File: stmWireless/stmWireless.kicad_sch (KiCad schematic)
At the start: 51 parts, among them IC1 BALFLB-WL-08D3, J1 SWD, J2 CORTEX_DEBUG, J3 Conn_02x08_Top_Bottom, J4 SMA, U1 STM32WLE5CBU6, U2 AP63203WU, U3 BGS12WN6E6327, Y1 Crystal_32MHz, Y2 Crystal_32.768kHz

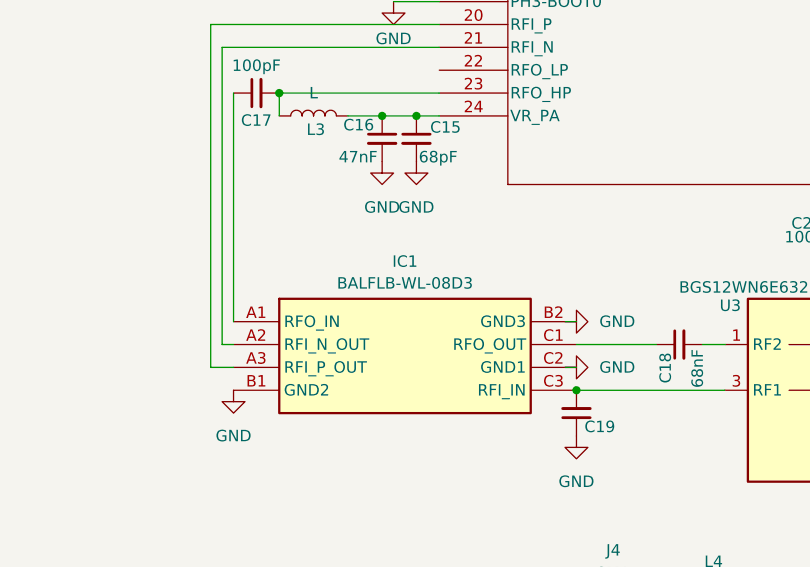
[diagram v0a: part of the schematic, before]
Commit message: substitute IPD to fix freqency
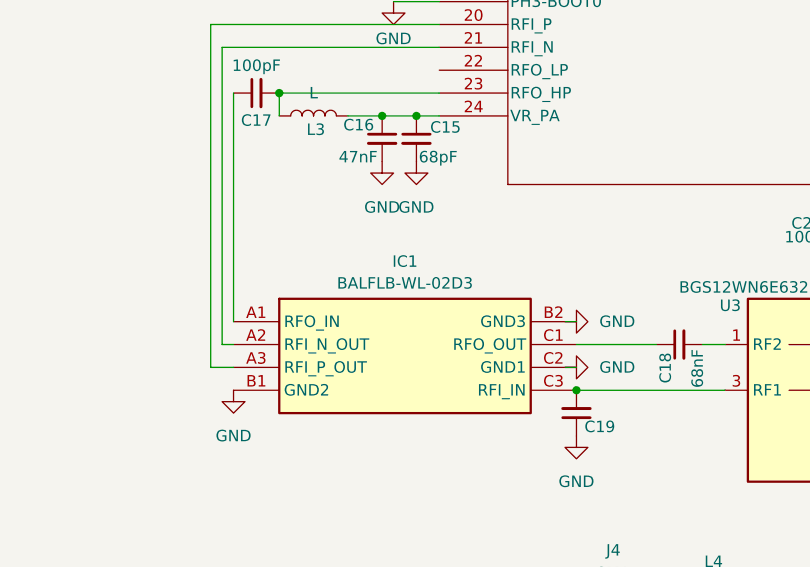
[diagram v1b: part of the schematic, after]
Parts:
- IC1: value BALFLB-WL-08D3 -> BALFLB-WL-02D3; footprint Project_library:BALFLBWL08D3 -> BALFHBWL02D3; symbol Project_library:BALFLB-WL-08D3 -> Project_library:BALFHB-WL-02D3; Manufacturer_Part_Number BALFLB-WL-08D3 -> BALFHB-WL-02D3; Mouser Part Number (none) -> 511-BALFHB-WL-02D3; Mouser Price/Stock (none) -> https://www.mouser.co.uk/ProductDetail/STMicroelectronics/B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
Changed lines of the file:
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@@
 	)
 	(symbol
-		(lib_id "Project_library:BALFLB-WL-08D3")
+		(lib_id "Project_library:BALFHB-WL-02D3")
 		(at 86.36 152.4 0)
 		(unit 1)
@@
 			)
 		)
-		(property "Value" "BALFLB-WL-08D3"
+		(property "Value" "BALFLB-WL-02D3"
 			(at 105.41 148.1398 0)
 			(effects
@@
 			)
 		)
-		(property "Footprint" "Project_library:BALFLBWL08D3"
+		(property "Footprint" "BALFHBWL02D3"
 			(at 120.65 247.32 0)
 			(effects
@@
 			)
 		)
-		(property "Datasheet" "https://www.st.com/resource/en/datasheet/balflb-wl-08d3.pdf"
+		(property "Datasheet" "https://www.st.com/resource/en/datasheet/balfhb-wl-02d3.pdf"
 			(at 120.65 347.32 0)
 			(effects
@@
 			)
 		)
-		(property "Description" "balun,filtering and matching of STM32WL 17dbm 490Mhz , QFN package 4 layers pcb"
+		(property "Description" "50  nominal input / conjugate matched balun to QFN-4L STM32WL in high power mode, 862-928 MHz with integrated harmonic filter"
 			(at 86.36 152.4 0)
 			(effects
@@
 			)
 		)
-		(property "Manufacturer_Part_Number" "BALFLB-WL-08D3"
+		(property "Manufacturer_Part_Number" "BALFHB-WL-02D3"
 			(at 120.65 747.32 0)
 			(effects
@@
 			)
 		)
-		(property "Mouser Part Number" ""
+		(property "Mouser Part Number" "511-BALFHB-WL-02D3"
 			(at 120.65 847.32 0)
 			(effects
@@
 			)
 		)
-		(property "Mouser Price/Stock" ""
+		(property "Mouser Price/Stock" "https://www.mouser.co.uk/ProductDetail/STMicroelectronics/BALFHB-WL-02D3?qs=T%252BzbugeAwjiiXP9WLIpAiQ%3D%3D"
 			(at 120.65 947.32 0)
 			(effects

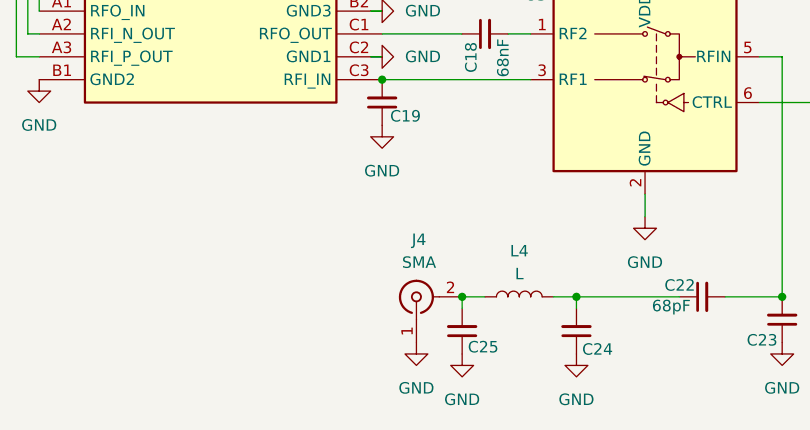
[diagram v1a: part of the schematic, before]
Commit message: fix backwards antenna
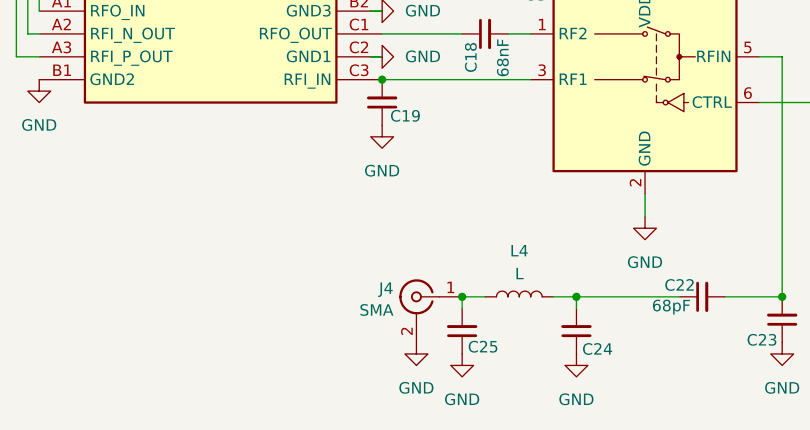
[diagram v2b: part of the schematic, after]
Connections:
- net GND: now also J4.2 (Ext); no longer J4.1 (In)
- net at C25.2, L4.1: now also J4.1 (In); no longer J4.2 (Ext)
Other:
- moved on the sheet: J4
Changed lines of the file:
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@@
 	)
 	(junction
+		(at 133.35 184.15)
+		(diameter 0)
+		(color 0 0 0 0)
+	)
+	(junction
 		(at 124.46 160.02)
 		(diameter 0)
@@
 	)
 	(junction
-		(at 133.35 184.15)
-		(diameter 0)
-		(color 0 0 0 0)
-	)
-	(junction
 		(at 245.11 59.69)
 		(diameter 0)
@@
 	(symbol
 		(lib_id "Connector:Conn_Coaxial")
-		(at 128.27 184.15 90)
+		(at 128.27 184.15 0)
+		(mirror y)
 		(unit 1)
 		(exclude_from_sim no)
@@
 		(on_board yes)
 		(dnp no)
-		(fields_autoplaced yes)
 		(property "Reference" "J4"
-			(at 128.5632 177.8 90)
+			(at 125.7299 183.231 0)
 			(effects
 				(font
 					(size 1.27 1.27)
 				)
+				(justify left)
 			)
 		)
 		(property "Value" "SMA"
-			(at 128.5632 180.34 90)
+			(at 125.7299 185.6553 0)
 			(effects
 				(font
 					(size 1.27 1.27)
 				)
+				(justify left)
 			)
 		)

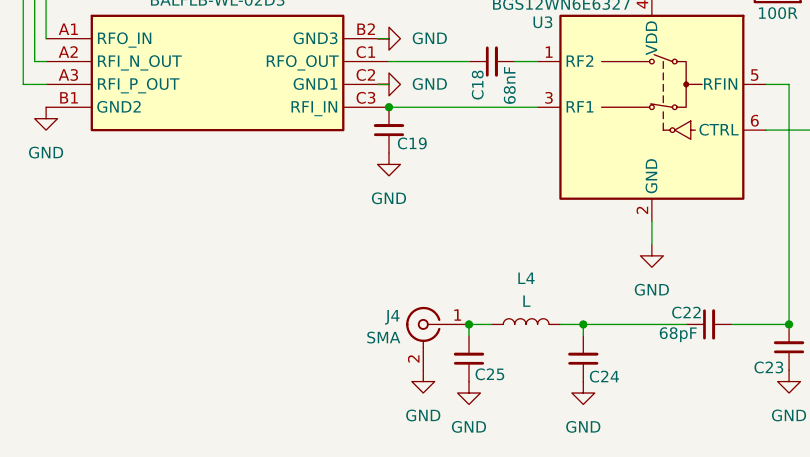
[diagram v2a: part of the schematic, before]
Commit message: add big reference manual that explains a lot and label 915mhz antenna
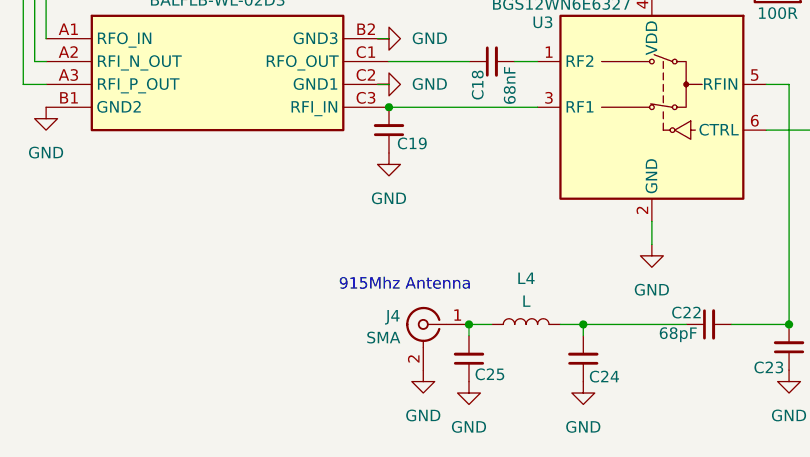
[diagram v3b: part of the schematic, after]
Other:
- note added: "915Mhz Antenna"
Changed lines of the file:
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@@
+		)
+	)
+	(text "915Mhz Antenna"
+		(exclude_from_sim no)
+		(at 126.238 179.832 0)
+		(effects
+			(font
+				(size 1.27 1.27)
+			)
 		)
 	)

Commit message: improve layout for power header and voltage regulator, and add i2c3 header
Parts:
- added J5: i2c3 header, Connector_PinHeader_2.54mm:PinHeader_2x05_P2.54mm_Vertical, symbol Connector_Generic:Conn_02x05_Odd_Even
- IC1: footprint BALFHBWL02D3 -> Project_library:BALFHBWL02D3
- J3: value Conn_02x08_Top_Bottom -> Power; symbol Connector_Generic:Conn_02x07_Top_Bottom -> Connector_Generic:Conn_02x07_Odd_Even
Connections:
- net GND: now also J3.10 (Pin_10), J3.12 (Pin_12), J3.14 (Pin_14), J3.4 (Pin_4), J3.6 (Pin_6), J5.7 (Pin_7), J5.8 (Pin_8); no longer J3.1 (Pin_1), J3.9 (Pin_9)
- net VBAT: no longer J3.14 (Pin_14)
- net VDD: now also J3.1 (Pin_1), J3.5 (Pin_5), J5.5 (Pin_5), J5.6 (Pin_6); no longer J3.10 (Pin_10), J3.11 (Pin_11), J3.4 (Pin_4)
- net VIN: now also J3.11 (Pin_11), J3.9 (Pin_9); no longer J3.12 (Pin_12), J3.5 (Pin_5), J3.6 (Pin_6)
- net i2c3_SCL: now reaches U1.15 (PA7)
- net i2c3_SCL: now also J5.1 (Pin_1), J5.2 (Pin_2)
- net i2c3_SDA: now reaches U1.2 (PB4)
- net i2c3_SDA: now also J5.3 (Pin_3), J5.4 (Pin_4)
- net i2c3_SMBA: now reaches U1.31 (PB2)
- net i2c3_SMBA: now also J5.10 (Pin_10), J5.9 (Pin_9)

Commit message: add GPIO port of most unused pins
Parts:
- added J6: GPIO1, Connector_PinHeader_2.54mm:PinHeader_1x13_P2.54mm_Vertical, symbol Connector_Generic:Conn_01x13
- added R10: 4.k7, Resistor_SMD:R_0603_1608Metric, symbol Device:R_Small
- added R9: 4.7k, Resistor_SMD:R_0603_1608Metric, symbol Device:R_Small
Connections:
- net VDD: now also R10.1, R9.1
- net i2c3_SCL: now also R9.2
- net i2c3_SDA: now also R10.2
- net at U1.10 (PA3): now also J6.8 (Pin_8)
- net at U1.12 (PA4): now also J6.9 (Pin_9)
- net at U1.13 (PA5): now also J6.10 (Pin_10)
- net at U1.14 (PA6): now also J6.11 (Pin_11)
- net at U1.16 (PA8): now also J6.12 (Pin_12)
- net at U1.17 (PA9): now also J6.13 (Pin_13)
- net at U1.3 (PB5): now also J6.1 (Pin_1)
- net at U1.4 (PB6): now also J6.2 (Pin_2)
- net at U1.5 (PB7): now also J6.3 (Pin_3)
- net at U1.6 (PB8): now also J6.4 (Pin_4)
- net at U1.7 (PA0): now also J6.5 (Pin_5)
- net at U1.8 (PA1): now also J6.6 (Pin_6)
- net at U1.9 (PA2): now also J6.7 (Pin_7)

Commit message: improve highlighted notes on datasheet, and add additional reference about impedance matching networks. Also add pin labels to schematic and PCB GPIO pins
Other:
- note added: "PB5 PB6 PB7 PB8 PA0 PA1 PA2 PA3 PA4 PA5 PA6 PA8 PA9"
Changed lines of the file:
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@@
+		)
+	)
+	(text "PB5\nPB6\nPB7\nPB8\nPA0\nPA1\nPA2\nPA3\nPA4\nPA5\nPA6\nPA8\nPA9"
+		(exclude_from_sim no)
+		(at 75.946 91.44 0)
+		(effects
+			(font
+				(size 1.6 1.6)
+			)
 		)
 	)
@@
 		(dnp no)
 		(property "Reference" "J6"
-			(at 77.978 90.2278 0)
+			(at 81.026 73.7178 0)
 			(effects
 				(font
@@
 		)
 		(property "Value" "GPIO1"
-			(at 77.978 92.6521 0)
-			(effects
-				(font
+			(at 84.328 110.6861 0)
+			(effects
+				(font

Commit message: initial layout of radio portion, add another reference design with BOM. still need to adjust impedance and add connector
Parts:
- L3: value L -> 47nH; footprint (none) -> Inductor_SMD:L_0603_1608Metric
- L4: value L -> 0R; footprint (none) -> Inductor_SMD:L_0603_1608Metric
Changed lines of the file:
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@@
 	(label "SWDIO"
 		(at 186.69 104.14 180)
-		(fields_autoplaced yes)
 		(effects
 			(font
@@
 	(label "JTDO"
 		(at 264.16 59.69 180)
-		(fields_autoplaced yes)
 		(effects
 			(font
@@
 	(label "SWCLK"
 		(at 186.69 88.9 180)
-		(fields_autoplaced yes)
 		(effects
 			(font
@@
 	(label "i2c3_SMBA"
 		(at 190.5 116.84 180)
-		(fields_autoplaced yes)
 		(effects
 			(font
@@
 	(label "JTDI"
 		(at 186.69 86.36 180)
-		(fields_autoplaced yes)
 		(effects
 			(font
@@
 	(label "JTDO"
 		(at 104.14 71.12 0)
-		(fields_autoplaced yes)
 		(effects
 			(font
@@
 	(label "JTDI"
 		(at 264.16 62.23 180)
-		(fields_autoplaced yes)
 		(effects
 			(font
@@
 	(label "SWDIO"
 		(at 264.16 54.61 180)
-		(fields_autoplaced yes)
 		(effects
 			(font
@@
 	(label "i2c3_SCL"
 		(at 35.56 77.47 0)
-		(fields_autoplaced yes)
 		(effects
 			(font
@@
 	(label "SWDIO"
 		(at 233.68 66.04 90)
-		(fields_autoplaced yes)
 		(effects
 			(font
@@
 	(label "i2c3_SDA"
 		(at 101.6 73.66 0)
-		(fields_autoplaced yes)
 		(effects
 			(font
@@
 	(label "VBAT"
 		(at 186.69 101.6 180)
-		(fields_autoplaced yes)
 		(effects
 			(font
@@
 	(label "SWCLK"
 		(at 228.6 66.04 90)
-		(fields_autoplaced yes)
 		(effects
 			(font
@@
 	(label "SWCLK"
 		(at 264.16 57.15 180)
-		(fields_autoplaced yes)
 		(effects
 			(font
@@
 	(label "NRST"
 		(at 264.16 64.77 180)
-		(fields_autoplaced yes)
 		(effects
 			(font
@@
 	(label "i2c3_SCL"
 		(at 101.6 106.68 0)
-		(fields_autoplaced yes)
 		(effects
 			(font
@@
 	(label "i2c3_SMBA"
 		(at 35.56 87.63 0)
-		(fields_autoplaced yes)
 		(effects
 			(font
@@
 	(label "i2c3_SDA"
 		(at 35.56 80.01 0)
-		(fields_autoplaced yes)
 		(effects
 			(font
@@
 	(label "VBAT"
 		(at 53.34 41.91 0)
-		(fields_autoplaced yes)
 		(effects
 			(font
@@
 	(label "NRST"
 		(at 104.14 114.3 0)
-		(fields_autoplaced yes)
 		(effects
 			(font
@@
 			)
 		)
-		(property "Value" "L"
+		(property "Value" "47nH"
 			(at 95.25 127 90)
 			(effects
@@
 			)
 		)
-		(property "Footprint" ""
+		(property "Footprint" "Inductor_SMD:L_0603_1608Metric"
 			(at 95.25 129.54 0)
 			(effects
@@
 			)
 		)
-		(property "Value" "L"
+		(property "Value" "0R"
 			(at 139.7 181.61 90)
 			(effects
@@
 			)
 		)
-		(property "Footprint" ""
+		(property "Footprint" "Inductor_SMD:L_0603_1608Metric"
 			(at 139.7 184.15 0)
 			(effects
